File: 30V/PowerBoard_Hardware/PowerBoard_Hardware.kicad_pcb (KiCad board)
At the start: 2 copper layers, 142 x 139.7 mm, 150 parts, among them Q1 Q_NMOS_GDS, Q10 Q_NMOS_GDS, Q2 Q_NMOS_GDS, Q3 Q_NMOS_GDS, Q4 Q_NMOS_GDS, Q5 Q_NMOS_GDS, Q6 Q_NMOS_GDS, Q7 Q_NMOS_GDS, Q8 Q_NMOS_GDS, Q9 Q_NMOS_GDS, U1 LT1910, U10 LT1910, U11 LT1910, U12 ACS722xLCTR-40AU, U13 ACS722xLCTR-40AU, U14 ACS722xLCTR-40AU, U15 OKI_5V, U16 OKI_3V3, U17 LT1910, U18 LT1910, U19 ACS722xLCTR-40AU, U2 LT1910, U20 ACS722xLCTR-40AU, U21 LT1910, U22 ACS722xLCTR-40AU, U3 LT1910, U4 LT1910, U5 ACS722xLCTR-40AU, U6 ACS722xLCTR-40AU, U7 ACS722xLCTR-40AU, U8 ACS722xLCTR-40AU, U9 LT1910

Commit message: fixed schematic b/c Zac made fun of me
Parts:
- moved C22 1.27 mm to (158.8, 120.0)
- moved C25 1.27 mm to (158.8, 96.5)
- moved C26 1.27 mm to (176.5, 108.6)
- moved C27 1.27 mm to (176.5, 132.1)
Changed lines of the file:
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@@
   )
   (module Capacitor_THT:CP_Radial_D12.5mm_P5.00mm (layer F.Cu)
-    (at 157.48 120.015)
+    (at 158.75 120.015)
     (descr "CP, Radial series, Radial, pin pitch=5.00mm, , diameter=12.5mm, Electrolytic Capacitor")
     (tags "CP Radial series Radial pin pitch 5.00mm  diameter 12.5mm Electrolytic Capacitor")
-    (fp_text reference C22 (at -4.953 -0.127 270) (layer F.SilkS)
+    (fp_text reference C22 (at 10.795 0) (layer F.SilkS)
       (effects (font (size 1 1) (thickness 0.15)))
     )
@@
   )
   (module Capacitor_THT:CP_Radial_D12.5mm_P5.00mm (layer F.Cu)
-    (at 157.48 96.52)
+    (at 158.75 96.52)
     (descr "CP, Radial series, Radial, pin pitch=5.00mm, , diameter=12.5mm, Electrolytic Capacitor")
     (tags "CP Radial series Radial pin pitch 5.00mm  diameter 12.5mm Electrolytic Capacitor")
-    (fp_text reference C25 (at -5.715 0) (layer F.SilkS)
+    (fp_text reference C25 (at 10.795 0) (layer F.SilkS)
       (effects (font (size 1 1) (thickness 0.15)))
     )
@@
   )
   (module Capacitor_THT:CP_Radial_D12.5mm_P5.00mm (layer F.Cu)
-    (at 177.8 108.585 180)
+    (at 176.53 108.585 180)
     (descr "CP, Radial series, Radial, pin pitch=5.00mm, , diameter=12.5mm, Electrolytic Capacitor")
     (tags "CP Radial series Radial pin pitch 5.00mm  diameter 12.5mm Electrolytic Capacitor")
-    (fp_text reference C26 (at -5.715 0.127) (layer F.SilkS)
+    (fp_text reference C26 (at 10.795 0.127) (layer F.SilkS)
       (effects (font (size 1 1) (thickness 0.15)))
     )
@@
   )
   (module Capacitor_THT:CP_Radial_D12.5mm_P5.00mm (layer F.Cu)
-    (at 177.8 132.08 180)
+    (at 176.53 132.08 180)
     (descr "CP, Radial series, Radial, pin pitch=5.00mm, , diameter=12.5mm, Electrolytic Capacitor")
     (tags "CP Radial series Radial pin pitch 5.00mm  diameter 12.5mm Electrolytic Capacitor")
-    (fp_text reference C27 (at -4.953 0 270) (layer F.SilkS)
-      (effects (font (size 1 1) (thickness 0.15)))
-    )
+    (fp_text reference C27 (at 10.795 0) (layer F.SilkS)
+      (effects (font (size 1 1) (thickness 0.15)))
+    )

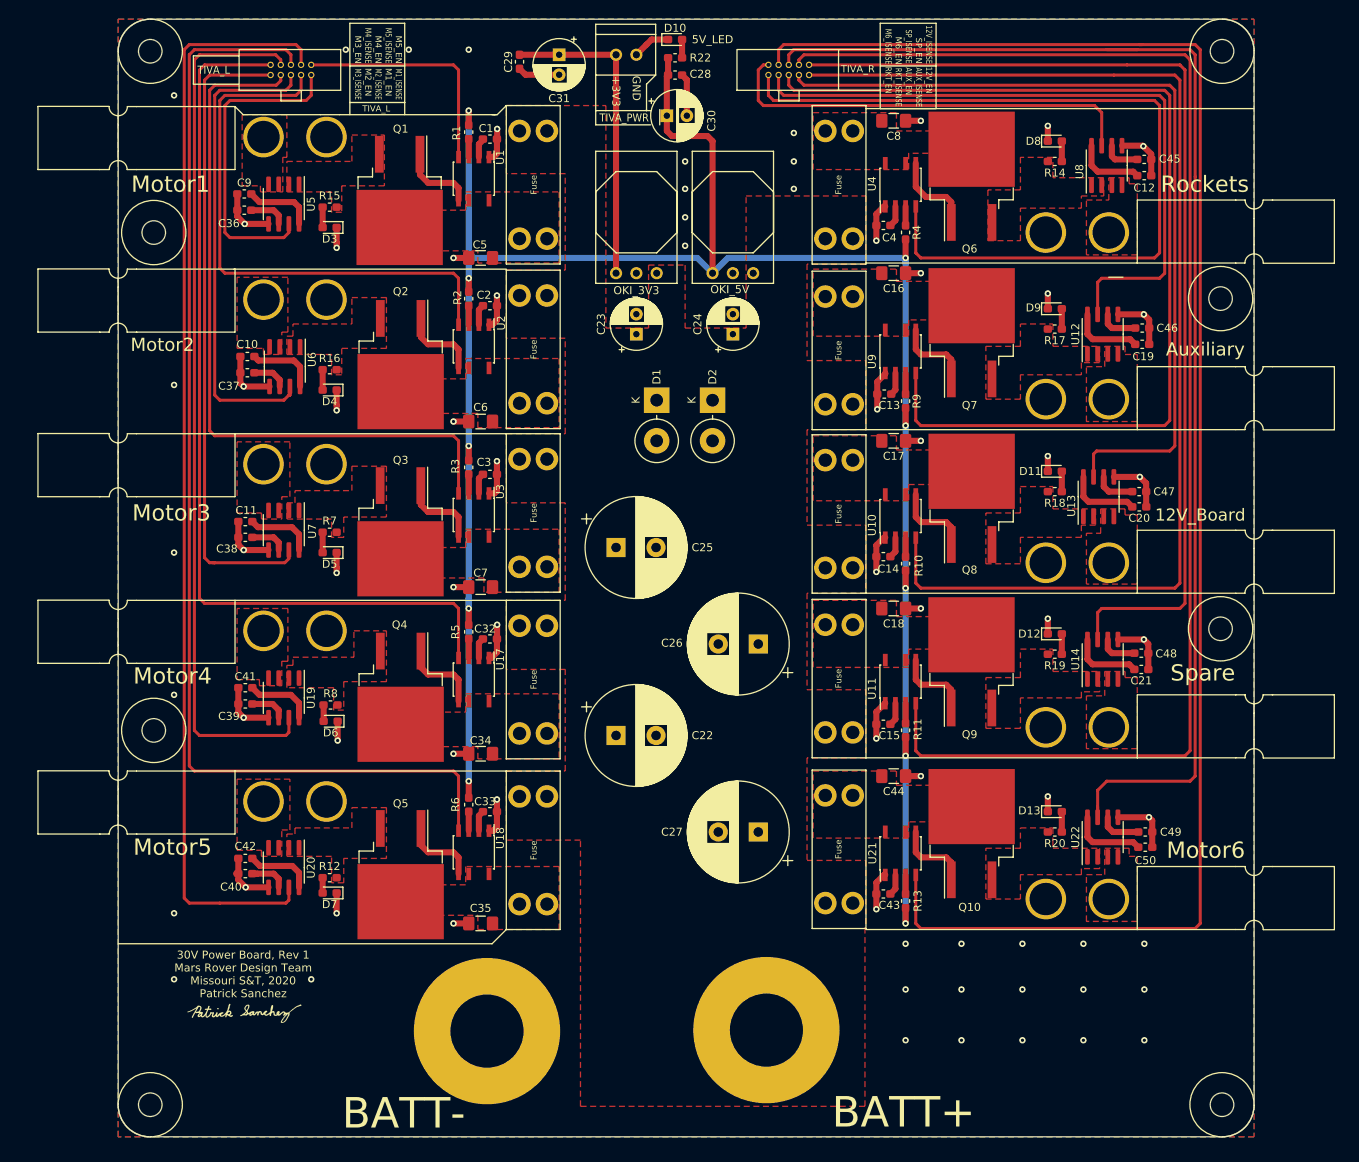
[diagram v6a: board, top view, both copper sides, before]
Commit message: Left side current sensors have 3.3V
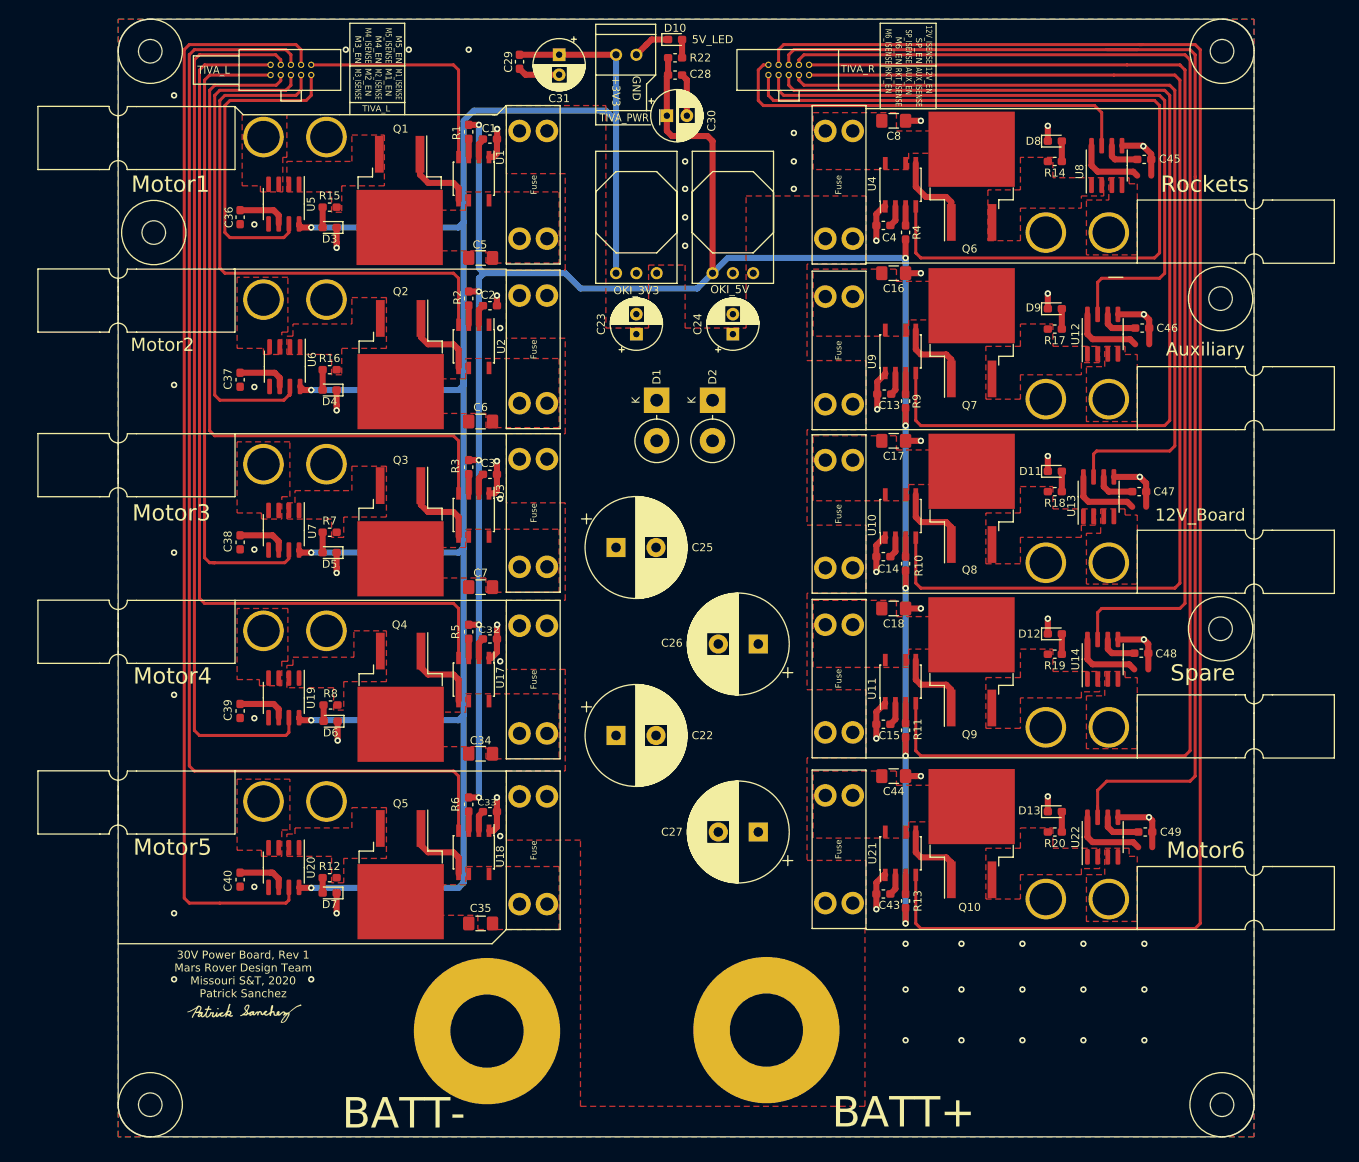
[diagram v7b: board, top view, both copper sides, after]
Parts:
- removed C10, C11, C12, C19, C20, C21, C41, C42, C50, C9: 0.1uF, Capacitor_SMD:C_0603_1608Metric_Pad1.05x0.95mm_HandSolder
- removed the REF** at (101.0, 119.4)
- moved C37 1.26 mm to (111.8, 75.6), turned to 270 degrees
- moved C39 1.09 mm to (111.8, 117.0), turned to 270 degrees
- moved C36 1.02 mm to (111.8, 55.2), turned to 270 degrees
- moved C40 0.99 mm to (111.8, 138.0), turned to 270 degrees
- moved C38 0.90 mm to (111.8, 95.9), turned to 270 degrees
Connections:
- U12 pad 8: Net-(C19-Pad1) -> +3V3
- U13 pad 8: Net-(C20-Pad1) -> +3V3
- U14 pad 8: Net-(C21-Pad1) -> +3V3
- U19 pad 8: Net-(C41-Pad1) -> +3V3
- U20 pad 8: Net-(C42-Pad1) -> +3V3
- U22 pad 8: Net-(C50-Pad1) -> +3V3
- U5 pad 8: Net-(C9-Pad1) -> +3V3
- U6 pad 8: Net-(C10-Pad1) -> +3V3
- U7 pad 8: Net-(C11-Pad1) -> +3V3
- U8 pad 8: Net-(C12-Pad1) -> +3V3
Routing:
- net +3V3: track 39.4 -> 305.4 mm, vias 0 -> 5
- net GND: track 175.5 -> 127.7 mm, vias 72 -> 71
- net Net-(C50-Pad1): track 9.35 -> 0.00 mm
- net Net-(C20-Pad1): track 9.11 -> 0.00 mm
- net Net-(C19-Pad1): track 8.97 -> 0.00 mm
- net Net-(C21-Pad1): track 8.86 -> 0.00 mm
- net Net-(C9-Pad1): track 8.75 -> 0.00 mm
- net Net-(C12-Pad1): track 8.72 -> 0.00 mm
- net Net-(C10-Pad1): track 8.72 -> 0.00 mm
- net Net-(C41-Pad1): track 8.47 -> 0.00 mm
- net Net-(C11-Pad1): track 8.47 -> 0.00 mm
- net Net-(C42-Pad1): track 8.42 -> 0.00 mm
- net +5V: track 277.3 -> 272.7 mm
- net Net-(C37-Pad1): track 4.37 -> 6.29 mm
- net Net-(C38-Pad1): track 4.52 -> 6.22 mm
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
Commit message: All 3V3 connected, need to fix silkscreen and move connectors
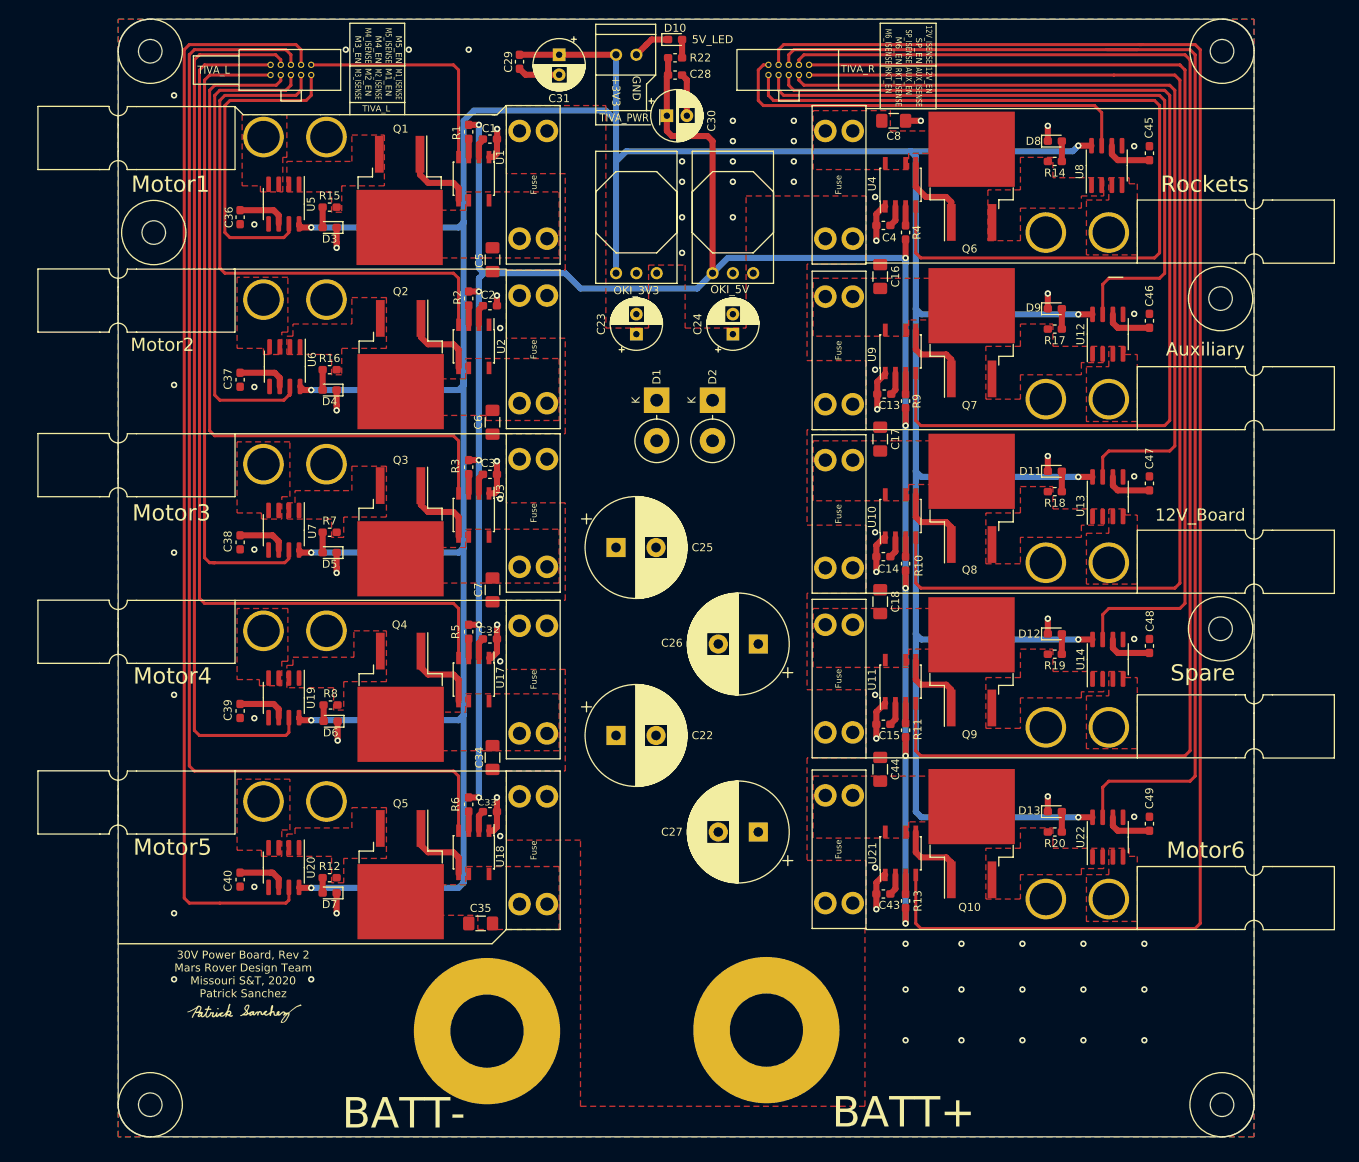
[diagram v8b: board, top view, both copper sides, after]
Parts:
- moved C18 1.89 mm to (191.8, 103.3), turned to 90 degrees
- moved C44 1.89 mm to (191.8, 124.2), turned to 90 degrees
- moved C16 1.74 mm to (191.8, 62.6), turned to 90 degrees
- moved C17 1.70 mm to (191.8, 83.0), turned to 90 degrees
- moved C47 1.65 mm to (225.4, 88.5), turned to 90 degrees
- moved C34 1.56 mm to (143.3, 122.8), turned to 270 degrees
- moved C7 1.53 mm to (143.3, 101.8), turned to 270 degrees
- moved C5 1.50 mm to (143.3, 60.5), turned to 270 degrees
- moved C6 1.49 mm to (143.3, 80.9), turned to 270 degrees
- moved C48 1.36 mm to (225.4, 108.8), turned to 90 degrees
- moved C46 1.28 mm to (225.4, 68.2), turned to 90 degrees
- moved C49 1.15 mm to (225.4, 131.1), turned to 90 degrees
- moved U13 1.14 mm to (220.2, 90.2)
- moved C45 1.01 mm to (225.4, 47.2), turned to 90 degrees
- moved U12 0.63 mm to (220.2, 69.8)
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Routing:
- net +3V3: track 305.4 -> 493.0 mm, vias 5 -> 10
- net GND: track 127.7 -> 83.7 mm, vias 71 -> 78
- net M6_ISENSE: track 164.2 -> 162.5 mm
- net Net-(C45-Pad1): track 4.66 -> 6.08 mm
- net 12V_ISENSE: track 106.0 -> 104.7 mm
- net Net-(C48-Pad1): track 4.73 -> 5.90 mm
- net Net-(C46-Pad1): track 4.84 -> 5.90 mm
- net Net-(C47-Pad1): track 5.02 -> 5.90 mm
- net SP_ISENSE: track 128.7 -> 127.9 mm
- net AUX_ISENSE: track 85.1 -> 84.4 mm
- net Net-(C49-Pad1): track 5.28 -> 5.90 mm
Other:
- board text added: "30V Power Board, Rev 2 Mars Rover Design Team Missouri S&T, 2020 Patrick Sanchez"
- board text removed: "30V Power Board, Rev 1 Mars Rover Design Team Missouri S&T, 2020 Patrick Sanchez"
